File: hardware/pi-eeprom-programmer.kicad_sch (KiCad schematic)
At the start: 3 parts, among them J1 Raspberry Pi GPIO Connector, J2 Conn_01x03, U1 ZIF Socket

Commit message: Updated board to reuse GPIO 2 & 3 for Chardev switch
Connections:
- removed net #20: J1.38 (Pin_38), J1.5 (Pin_5), J2.2 (Pin_2), U1.16 (D4), U1.26 (A13)
- net #21 renamed SDA
- net SDA: no longer J1.40 (Pin_40)
- new net SCL: J1.5 (Pin_5), U1.16 (D4)
- new net SW_SEL: J2.2 (Pin_2), U1.26 (A13)
- no-connect marks 8 -> 10
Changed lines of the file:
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@@
   (title_block
     (title "Pi EEProm Programmer")
-    (date "2023-08-08")
-    (rev "0.9.0")
+    (date "2023-08-16")
+    (rev "0.9.1")
   )
   (no_connect (at 100.33 66.04))
+  (no_connect (at 100.33 109.22))
   (no_connect (at 100.33 104.14))
   (no_connect (at 87.63 73.66))
@@
   (no_connect (at 100.33 78.74))
   (no_connect (at 87.63 83.82))
+  (no_connect (at 100.33 111.76))
   (wire (pts (xy 161.29 80.01) (xy 172.72 80.01))
     (stroke (width 0) (type default) (color 0 0 0 0))
@@
     (stroke (width 0) (type default) (color 0 0 0 0))
   )
-  (wire (pts (xy 110.49 111.76) (xy 100.33 111.76))
-    (stroke (width 0) (type default) (color 0 0 0 0))
-  )
   (wire (pts (xy 166.37 74.93) (xy 172.72 74.93))
     (stroke (width 0) (type default) (color 0 0 0 0))
@@
   )
   (wire (pts (xy 72.39 76.2) (xy 87.63 76.2))
-    (stroke (width 0) (type default) (color 0 0 0 0))
-  )
-  (wire (pts (xy 105.41 109.22) (xy 100.33 109.22))
     (stroke (width 0) (type default) (color 0 0 0 0))
   )
@@
     )
   )
-  (global_label "SW_SEL" (shape input) (at 219.71 74.93 270) (fields_autoplaced)
-    (effects (font (size 1.27 1.27)) (justify right))
-    (property "Intersheet References" "${INTERSHEET_REFS}" (id 0) (at 219.6306 84.2694 90)
-      (effects (font (size 1.27 1.27)) (justify right) hide)
+  (global_label "SCL" (shape input) (at 222.25 74.93 0) (fields_autoplaced)
+    (effects (font (size 1.27 1.27)) (justify left))
+    (property "Intersheet References" "${INTERSHEET_REFS}" (id 0) (at 228.0818 75.0094 0)
+      (effects (font (size 1.27 1.27)) (justify left) hide)
     )
   )
@@
     )
   )
-  (global_label "SDA" (shape bidirectional) (at 215.9 72.39 90) (fields_autoplaced)
-    (effects (font (size 1.27 1.27)) (justify left))
-    (property "Intersheet References" "${INTERSHEET_REFS}" (id 0) (at 215.8206 66.4977 90)
+  (global_label "SDA" (shape bidirectional) (at 218.44 72.39 0) (fields_autoplaced)
+    (effects (font (size 1.27 1.27)) (justify left))
+    (property "Intersheet References" "${INTERSHEET_REFS}" (id 0) (at 224.3323 72.3106 0)
       (effects (font (size 1.27 1.27)) (justify left) hide)
     )
@@
     )
   )
-  (global_label "#20" (shape input) (at 105.41 109.22 0) (fields_autoplaced)
-    (effects (font (size 1.27 1.27)) (justify left))
-    (property "Intersheet References" "${INTERSHEET_REFS}" (id 0) (at 0 0 0)
-      (effects (font (size 1.27 1.27)) hide)
-    )
-  )
   (global_label "#16" (shape input) (at 208.28 77.47 0) (fields_autoplaced)
     (effects (font (size 1.27 1.27)) (justify left))
@@
     )
   )
-  (global_label "#21" (shape input) (at 110.49 111.76 0) (fields_autoplaced)
-    (effects (font (size 1.27 1.27)) (justify left))
-    (property "Intersheet References" "${INTERSHEET_REFS}" (id 0) (at 0 0 0)
-      (effects (font (size 1.27 1.27)) hide)
-    )
-  )
   (global_label "MOSI" (shape input) (at 156.21 77.47 180) (fields_autoplaced)
     (effects (font (size 1.27 1.27)) (justify right))
@@
     )
   )
-  (global_label "#21" (shape input) (at 218.44 72.39 0) (fields_autoplaced)
-    (effects (font (size 1.27 1.27)) (justify left))
-    (property "Intersheet References" "${INTERSHEET_REFS}" (id 0) (at 20.32 0 0)
-      (effects (font (size 1.27 1.27)) hide)
-    )
-  )
   (global_label "GND" (shape input) (at 182.88 120.65 270) (fields_autoplaced)
     (effects (font (size 1.27 1.27)) (justify right))
@@
     )
   )
-  (global_label "SW_SEL" (shape output) (at 74.93 68.58 180) (fields_autoplaced)
-    (effects (font (size 1.27 1.27)) (justify right))
-    (property "Intersheet References" "${INTERSHEET_REFS}" (id 0) (at 65.5906 68.5006 0)
+  (global_label "SCL" (shape output) (at 74.93 68.58 180) (fields_autoplaced)
+    (effects (font (size 1.27 1.27)) (justify right))
+    (property "Intersheet References" "${INTERSHEET_REFS}" (id 0) (at 69.0982 68.5006 0)
       (effects (font (size 1.27 1.27)) (justify right) hide)
     )
@@
       (effects (font (size 1.27 1.27)) hide)
     )
-  )
-  (global_label "#20" (shape input) (at 222.25 74.93 0) (fields_autoplaced)
-    (effects (font (size 1.27 1.27)) (justify left))
-    (property "Intersheet References" "${INTERSHEET_REFS}" (id 0) (at 19.05 0 0)
-      (effects (font (size 1.27 1.27)) hide)
-    )

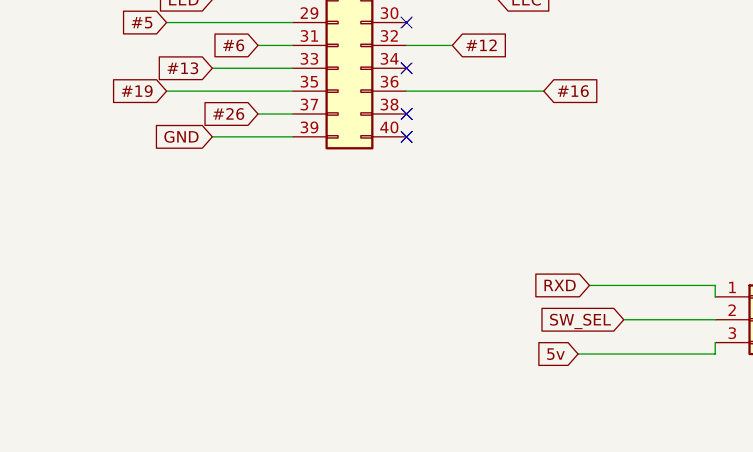
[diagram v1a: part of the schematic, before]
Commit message: Updated PCB to include spot for Serial EEPROM and updated README to reflect it
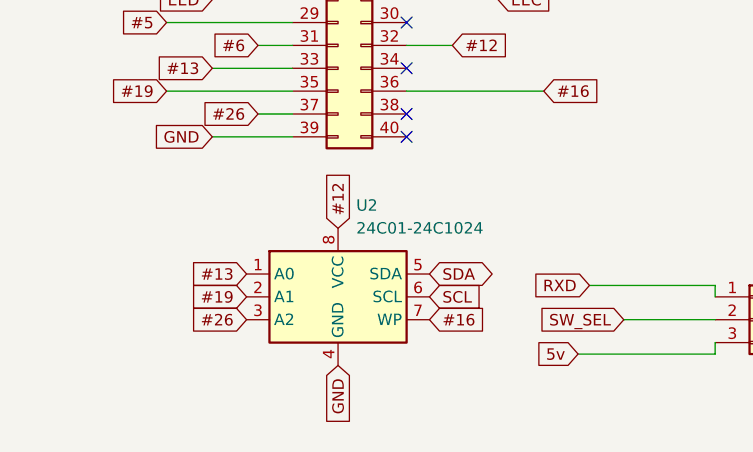
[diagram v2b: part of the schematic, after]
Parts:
- added U2: 24C01-24C1024, Package_DIP:DIP-8_W7.62mm_Socket, symbol Memory_EEPROM:CAT24C128
- U1: footprint Package_DIP:DIP-28_W15.24mm -> Package_DIP:DIP-28_W15.24mm_Socket
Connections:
- net #12: now also U2.8 (VCC)
- net #13: now also U2.1 (A0)
- net #16: now also U2.7 (WP)
- net #19: now also U2.2 (A1)
- net #26: now also U2.3 (A2)
- net GND: now also U2.4 (GND)
- net SCL: now also U2.6 (SCL)
- net SDA: now also U2.5 (SDA)
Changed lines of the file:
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@@
   (title_block
     (title "Pi EEProm Programmer")
-    (date "2023-08-16")
-    (rev "0.9.1")
+    (date "2023-08-20")
+    (rev "0.9.2")
   )
   (no_connect (at 100.33 66.04))
@@
     )
   )
+  (global_label "GND" (shape input) (at 92.71 137.16 270) (fields_autoplaced)
+    (effects (font (size 1.27 1.27)) (justify right))
+    (property "Intersheet References" "${INTERSHEET_REFS}" (id 0) (at -90.17 16.51 0)
+      (effects (font (size 1.27 1.27)) hide)
+    )
+  )
   (global_label "SCL" (shape input) (at 222.25 74.93 0) (fields_autoplaced)
     (effects (font (size 1.27 1.27)) (justify left))
@@
     )
   )
+  (global_label "#13" (shape input) (at 82.55 127 180) (fields_autoplaced)
+    (effects (font (size 1.27 1.27)) (justify right))
+    (property "Intersheet References" "${INTERSHEET_REFS}" (id 0) (at 3.81 22.86 0)
+      (effects (font (size 1.27 1.27)) hide)
+    )
+  )
   (global_label "GND1" (shape input) (at 166.37 110.49 180) (fields_autoplaced)
     (effects (font (size 1.27 1.27)) (justify right))
@@
     )
   )
+  (global_label "SCL" (shape input) (at 102.87 129.54 0) (fields_autoplaced)
+    (effects (font (size 1.27 1.27)) (justify left))
+    (property "Intersheet References" "${INTERSHEET_REFS}" (id 0) (at 108.7018 129.4606 0)
+      (effects (font (size 1.27 1.27)) (justify left) hide)
+    )
+  )
   (global_label "#16" (shape input) (at 208.28 77.47 0) (fields_autoplaced)
     (effects (font (size 1.27 1.27)) (justify left))
@@
     )
   )
+  (global_label "#19" (shape input) (at 82.55 129.54 180) (fields_autoplaced)
+    (effects (font (size 1.27 1.27)) (justify right))
+    (property "Intersheet References" "${INTERSHEET_REFS}" (id 0) (at 8.89 22.86 0)
+      (effects (font (size 1.27 1.27)) hide)
+    )
+  )
   (global_label "MOSI" (shape input) (at 156.21 77.47 180) (fields_autoplaced)
     (effects (font (size 1.27 1.27)) (justify right))
@@
     )
   )
+  (global_label "#26" (shape input) (at 82.55 132.08 180) (fields_autoplaced)
+    (effects (font (size 1.27 1.27)) (justify right))
+    (property "Intersheet References" "${INTERSHEET_REFS}" (id 0) (at -1.27 22.86 0)
+      (effects (font (size 1.27 1.27)) hide)
+    )
+  )
   (global_label "#25" (shape input) (at 110.49 88.9 0) (fields_autoplaced)
     (effects (font (size 1.27 1.27)) (justify left))
@@
     )
   )
+  (global_label "#16" (shape input) (at 102.87 132.08 0) (fields_autoplaced)
+    (effects (font (size 1.27 1.27)) (justify left))
+    (property "Intersheet References" "${INTERSHEET_REFS}" (id 0) (at -12.7 25.4 0)
+      (effects (font (size 1.27 1.27)) hide)
+    )
+  )
   (global_label "SCLK" (shape input) (at 73.66 91.44 180) (fields_autoplaced)
     (effects (font (size 1.27 1.27)) (justify right))
@@
     )
   )
+  (global_label "#12" (shape input) (at 92.71 121.92 90) (fields_autoplaced)
+    (effects (font (size 1.27 1.27)) (justify left))
+    (property "Intersheet References" "${INTERSHEET_REFS}" (id 0) (at -8.89 227.33 0)
+      (effects (font (size 1.27 1.27)) hide)
+    )
+  )
   (global_label "CE0" (shape input) (at 115.57 91.44 0) (fields_autoplaced)
     (effects (font (size 1.27 1.27)) (justify left))
@@
     (property "Intersheet References" "${INTERSHEET_REFS}" (id 0) (at 0 0 0)
       (effects (font (size 1.27 1.27)) hide)
+    )
+  )
+  (global_label "SDA" (shape bidirectional) (at 102.87 127 0) (fields_autoplaced)
+    (effects (font (size 1.27 1.27)) (justify left))
+    (property "Intersheet References" "${INTERSHEET_REFS}" (id 0) (at 108.7623 127.0794 0)
+      (effects (font (size 1.27 1.27)) (justify left) hide)
     )
   )
@@
     (property "Reference" "U1" (id 0) (at 182.88 55.0926 0))
     (property "Value" "ZIF Socket" (id 1) (at 182.88 57.404 0))
-    (property "Footprint" "Package_DIP:DIP-28_W15.24mm" (id 2) (at 182.88 87.63 0)
+    (property "Footprint" "Package_DIP:DIP-28_W15.24mm_Socket" (id 2) (at 182.88 87.63 0)
       (effects (font (size 1.27 1.27)) hide)
     )
@@
     (pin "9")
   )
+  (symbol (lib_id "Memory_EEPROM:CAT24C128") (at 92.71 129.54 0) (unit 1)
+    (in_bom yes) (on_board yes) (fields_autoplaced)
+    (property "Reference" "U2" (id 0) (at 94.7294 119.38 0)
+      (effects (font (size 1.27 1.27)) (justify left))
+    )
+    (property "Value" "24C01-24C1024" (id 1) (at 94.7294 121.92 0)
+      (effects (font (size 1.27 1.27)) (justify left))
+    )
+    (property "Footprint" "Package_DIP:DIP-8_W7.62mm_Socket" (id 2) (at 92.71 129.54 0)
+      (effects (font (size 1.27 1.27)) hide)
+    )
+    (property "Datasheet" "https://www.onsemi.com/pub/Collateral/CAT24C128-D.PDF" (id 3) (at 92.71 129.54 0)
+      (effects (font (size 1.27 1.27)) hide)
+    )
+    (pin "1")
+    (pin "2")
+    (pin "3")
+    (pin "4")
+    (pin "5")
+    (pin "6")
+    (pin "7")
+    (pin "8")
+  )
   (symbol (lib_id "Connector_Generic:Conn_01x03") (at 139.7 132.08 0) (unit 1)
     (in_bom yes) (on_board yes) (fields_autoplaced)
@@
     )
     (path "/00000000-0000-0000-0000-00006354a5d1"
-      (reference "U1") (unit 1) (value "ZIF Socket") (footprint "Package_DIP:DIP-28_W15.24mm")
-    )
-  )
+      (reference "U1") (unit 1) (value "ZIF Socket") (footprint "Package_DIP:DIP-28_W15.24mm_Socket")
+    )
+    (path "/48feab8d-d9a6-4d93-b3de-184b8ed4f1ca"
+      (reference "U2") (unit 1) (value "24C01-24C1024") (footprint "Package_DIP:DIP-8_W7.62mm_Socket")
+    )
+  )
